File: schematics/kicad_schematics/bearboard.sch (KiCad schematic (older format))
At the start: 61 parts

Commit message: Added new joy stick to the misc library and schematic
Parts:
- removed P?: CONN_10X2, symbol CONN_10X2
- removed R? (x4): 0, symbol R
- added C? (x5): 100nF, symbol C
- added D? (x4): LED, symbol LED
- added JP? (x2): CONN_3, symbol CONN_3
- added P?: KOBICONN, symbol JACK-PMS
- added R? (x4): 690?, symbol R
- added R? (x5): 10K, symbol R
- added R? (x5): 0, symbol R
- added U?: TACT-SKQU, symbol TACT-SKQU
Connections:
- net labels added: JOY_CENTER, JOY_DOWN, JOY_LEFT, JOY_RIGHT, JOY_UP, LED0, LED1, LED2, LED3, WIZ_BRDY3
- net labels removed: +3.3V, TRACE_CK, TRACE_D0, TRACE_D1, TRACE_D2, TRACE_D3, WIZ_BRD3
- wire segments 498 -> 523
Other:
- note added: "GPIO LEDs"
- note added: "GPS CONNECTOR"
- note added: "JOYSTICK_BUTTONS"
- note added: "Optional UART2 Connector"
- note added: "POWER SUPPLY"
- note removed: "CN10 will suppot both legacy JTAG and\nfuture JTAG by 0 ohm resistors."
- note removed: "TRACE CONNECTOR"
- moved on the sheet: D?, P?, R?, U?

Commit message: Cleaned up Schematic File and modified SD card module, bearboard schematic
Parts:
- removed SW? (x2): SWITCH_INV, symbol SWITCH_INV
- removed U?: SD_CARD, symbol SD_CARD
- added JP?: CONN_3, symbol CONN_3
- added SW5, SW6: SWITCH, symbol SWITCH
- added U14: SD_CARD, symbol SD_CARD
- gave numbers to parts that had none: 80
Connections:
- net labels added: ARD_SH_AREF, ARD_SH_GP_4, ARD_SH_GP_5, ARD_SH_GP_6, ARD_SH_GP_7, ARD_SH_GP_8, ARD_SH_GP_9, BOOT0, BOOT1, USB5V, USBFTDI5V, VREF+, VREF-
- net labels removed: A, USBFTDI, USBPWR
- wire segments 523 -> 536
- no-connect marks 5 -> 6
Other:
- note added: "ANALOG POWER SUPPLY"
- note added: "ARM ST103F MICROCONTROLLER"
- note added: "BATTERY CONNECTOR"
- note added: "BOOT SWITCHES"
- note added: "FTDI PROGRAM INTERFACE"
- note added: "MAIN CRYSTAL"
- note added: "PORT GPIO"
- note added: "REAL-TIME CLOCK"
- note added: "RESET SWITCH"
- note added: "USB SLAVE INTERFACE"
- note added: "WIZNET NETWORK INTERFACE"
- moved on the sheet: C1, C10, C11, C12, C13, C2, C3, C4, C5, C6, C7, C8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

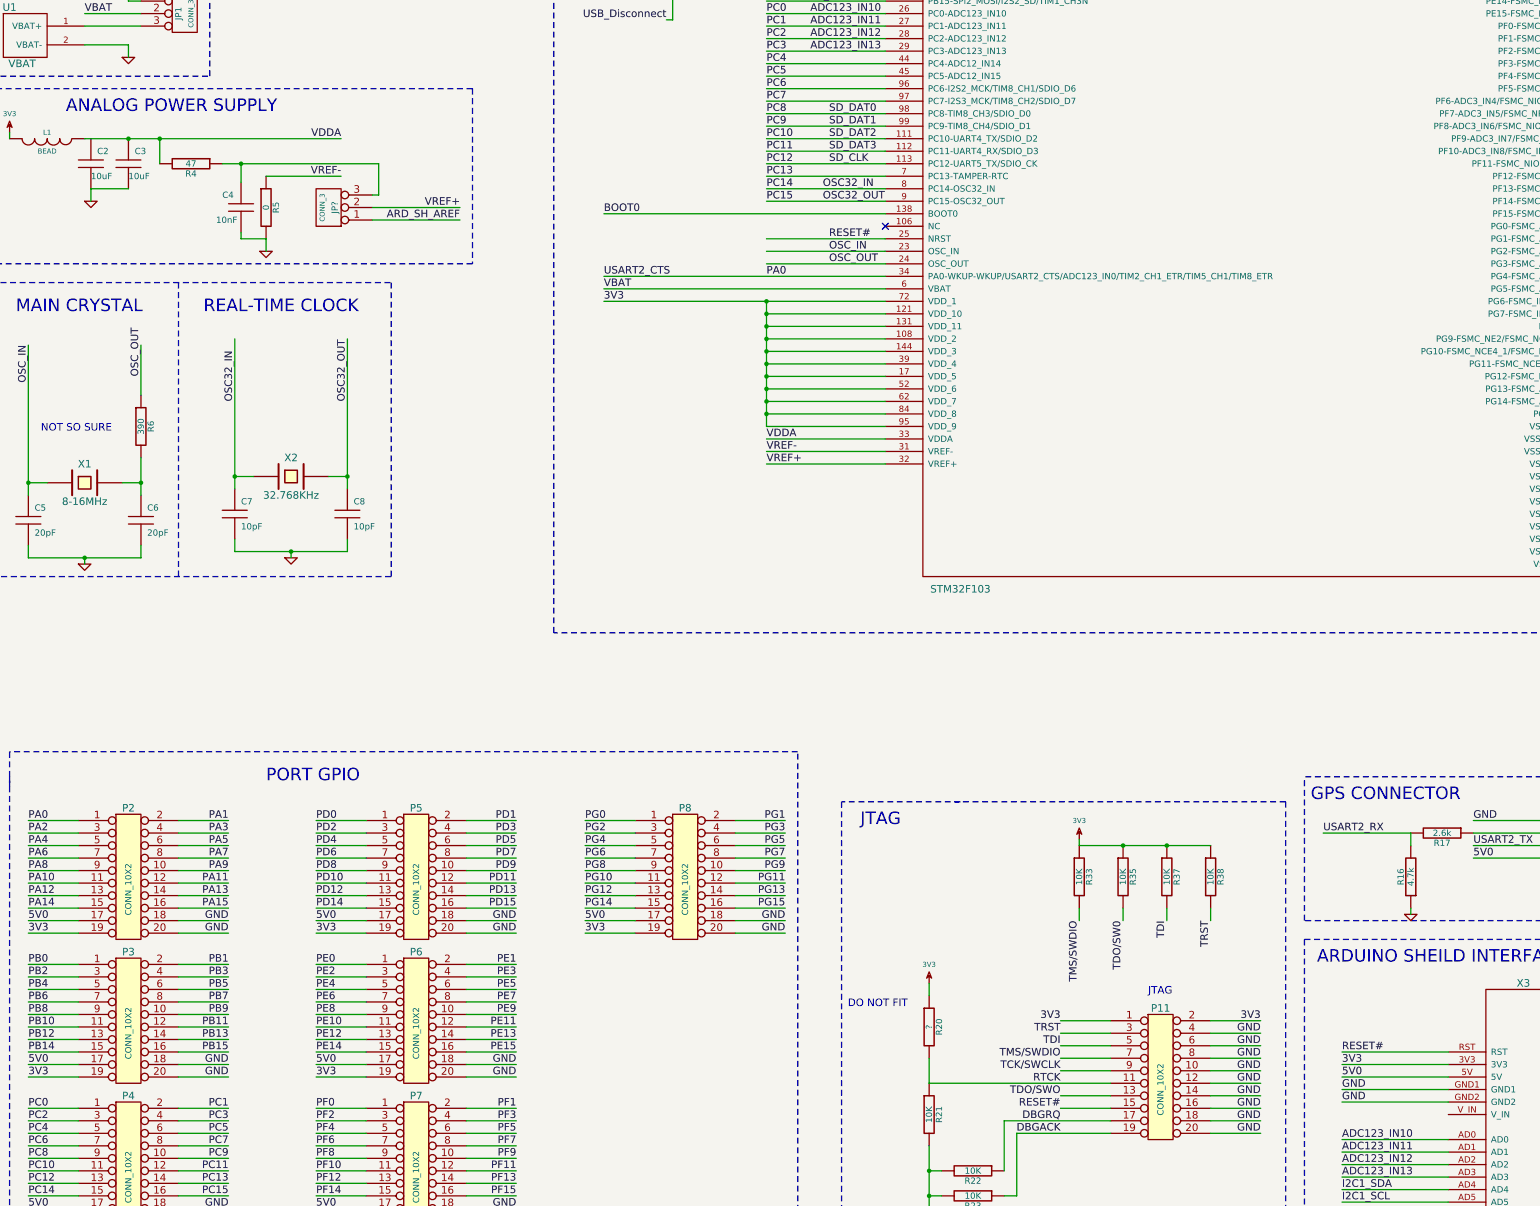
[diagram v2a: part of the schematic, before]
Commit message: Updated USB connector to change the sheild pin to power input Updated the schematic to fix some schematic electrical issues
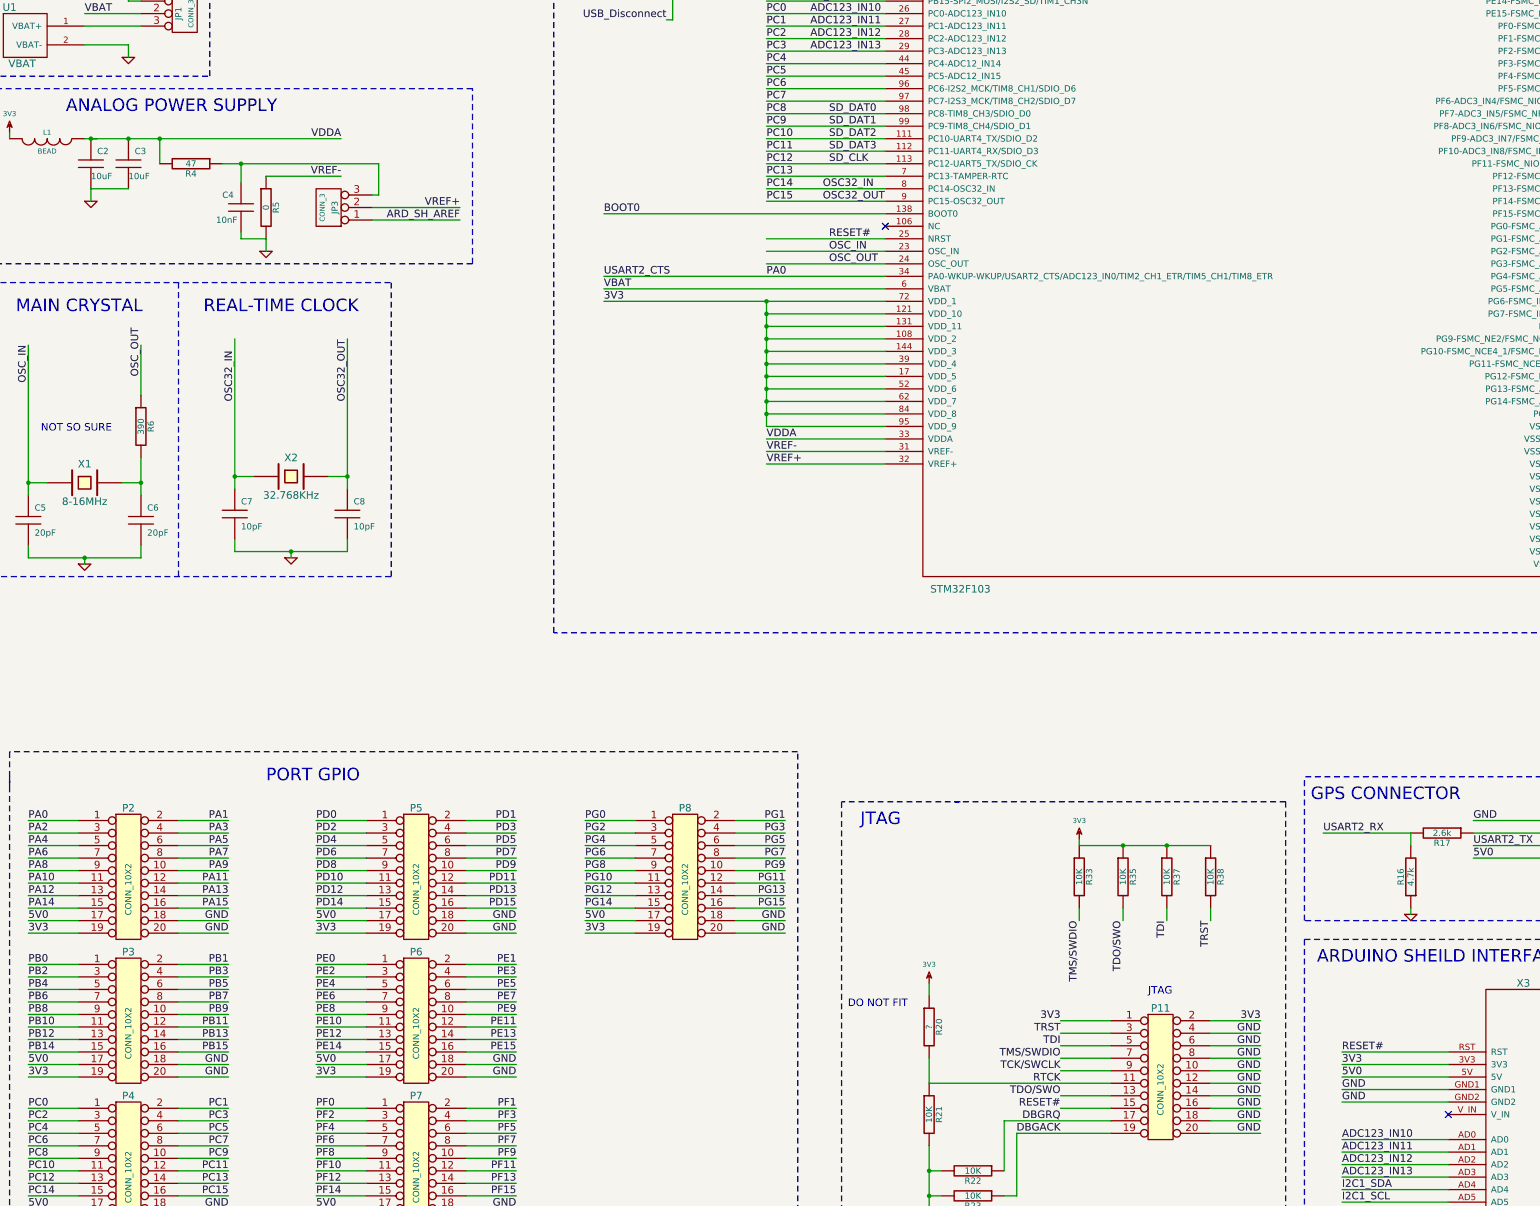
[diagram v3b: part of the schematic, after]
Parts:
- gave numbers to parts that had none: 1
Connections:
- net TDO/SW0 is gone; now on net PB3: R35.2
- net VDDA: now also C2.1
- no-connect marks 6 -> 7
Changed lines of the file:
@@
-EESchema Schematic File Version 2  date Wed 10 Mar 2010 05:32:05 PM EST
+EESchema Schematic File Version 2  date Wed 10 Mar 2010 08:20:30 PM EST
 LIBS:power
 LIBS:device
@@
 Sheet 1 5
 Title "BearBoard STM32F103"
-Date "10 mar 2010"
+Date "11 mar 2010"
 Rev "0"
 Comp "University of Maine"
@@
 Comment4 ""
 $EndDescr
+Text Label 9650 13600 3    60   ~ 0
+TDO/SWO
+Wire Wire Line
+	9650 13500 9650 13600
 Wire Notes Line
 	4450 8350 600  8350
 Wire Notes Line
-	4450 6950 4450 8350
+	4450 8350 4450 6950
 Wire Notes Line
 	4450 6950 600  6950
@@
 	10350 13600 10350 13500
 Wire Wire Line
-	9650 13600 9650 13500
-Wire Wire Line
 	9300 13600 9300 13500
 Connection ~ 10000 13000
@@
 Wire Wire Line
 	3650 8000 4350 8000
+Wire Wire Line
+	1400 7350 1450 7350
+Connection ~ 1400 7350
+NoConn ~ 12250 15150
 Text Label 4350 8000 2    60   ~ 0
 ARD_SH_AREF
 $Comp
-L CONN_3 JP?
+L CONN_3 JP3
 U 1 1 4B981D76
 P 3300 7900
-F 0 "JP?" V 3250 7900 50  0000 C CNN
+F 0 "JP3" V 3250 7900 50  0000 C CNN
 F 1 "CONN_3" V 3350 7900 40  0000 C CNN
 	1    3300 7900
@@
 Text Label 10350 13600 3    60   ~ 0
 TRST
-Text Label 9650 13600 3    60   ~ 0
-TDO/SW0
 Text Label 9300 13600 3    60   ~ 0
 TMS/SWDIO

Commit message: back annotated footprints into eeschem schematic
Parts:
- C1, C10, C11, C12, C13, C2, C3, C4, C5, C6, C7, C8, C9, R1, R10, R11, R12, R13, R14, R15, R16, R17, R18, R19, R2, R20, R21, R22, R23, R24, R25, R26, R27, R28, R29, R3, R30, R31, R32, R33, R34, R35, R36, R37, R38, R4, R5, R6, R7, R8, R9: footprint (none) -> SM0805
- D4, D5, D6, D7: footprint (none) -> LED-0805
- JP1, JP2, JP3: footprint (none) -> PIN_ARRAY_3X1
- P10: footprint (none) -> PIN_ARRAY_4x1
- P11, P2, P3, P4, P5, P6, P7, P8: footprint (none) -> PIN_ARRAY_10X2
- P9: footprint (none) -> PIN_ARRAY_7X1
- U2: footprint (none) -> LQFP144
- U3: footprint (none) -> alps_tact_button
- U4: footprint (none) -> EM406

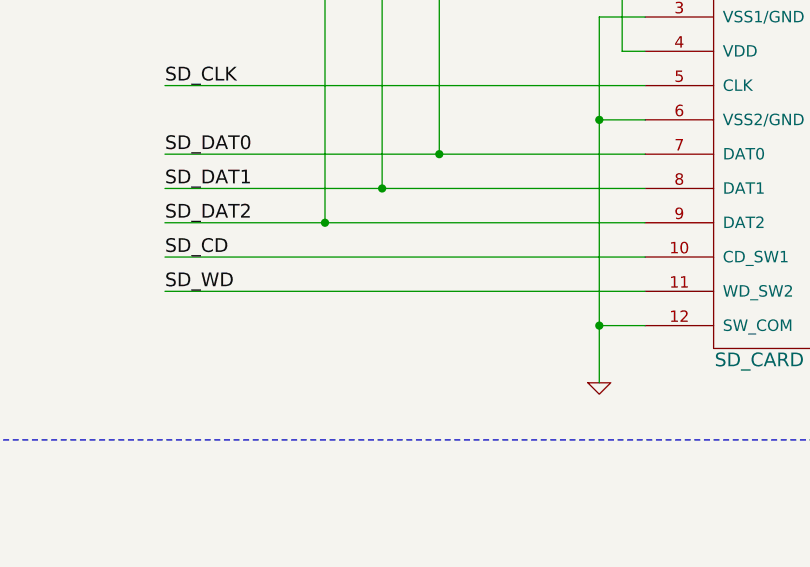
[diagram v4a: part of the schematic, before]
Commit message: added datasheets for cyrstals and aurdino sheild stuff
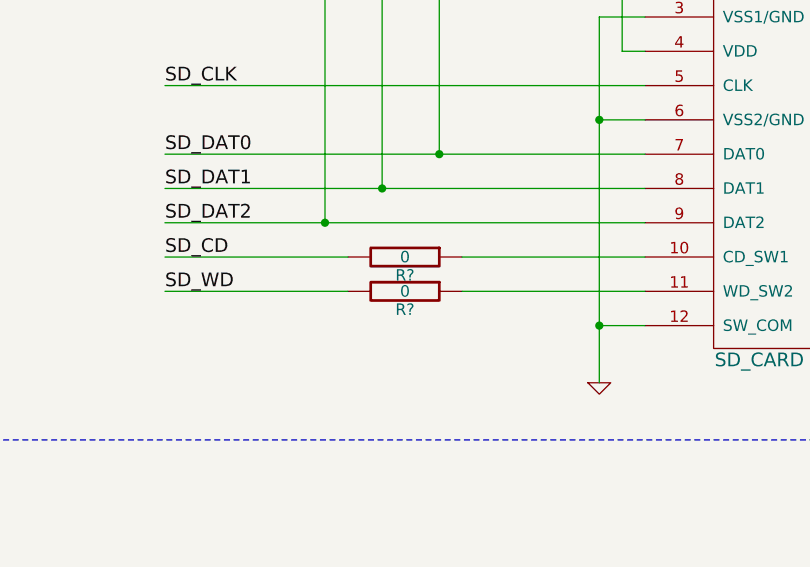
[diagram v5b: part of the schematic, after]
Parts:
- added R? (x2): 0, SM0805, symbol R
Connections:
- net PD13: now also R?.2; no longer U14.11 (WD_SW2)
- net PD3: now also R?.2; no longer U14.10 (CD_SW1)
- new net: R?.1, U14.10 (CD_SW1)
- new net: R?.1, U14.11 (WD_SW2)
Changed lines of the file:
@@
-EESchema Schematic File Version 2  date Fri 12 Mar 2010 11:31:07 AM EST
+EESchema Schematic File Version 2  date Sat 13 Mar 2010 12:50:25 PM EST
 LIBS:power
 LIBS:device
@@
 Sheet 1 5
 Title "BearBoard STM32F103"
-Date "11 mar 2010"
+Date "13 mar 2010"
 Rev "0"
 Comp "University of Maine"
@@
 Comment4 ""
 $EndDescr
-Text Label 9650 13600 3    60   ~ 0
-TDO/SWO
+Wire Wire Line
+	18600 11200 17800 11200
+Wire Wire Line
+	19100 11200 19900 11200
 Wire Wire Line
 	9650 13500 9650 13600
@@
 	7750 7450 6800 7450
 Wire Wire Line
-	17800 11200 19900 11200
-Wire Wire Line
 	17800 10900 19900 10900
 Wire Wire Line
@@
 	17800 10750 19900 10750
 Wire Wire Line
-	17800 11050 19900 11050
-Wire Wire Line
 	6800 7550 7750 7550
 Wire Wire Line
@@
 	1400 7350 1450 7350
 Connection ~ 1400 7350
+Wire Wire Line
+	19900 11050 19100 11050
+Wire Wire Line
+	18600 11050 17800 11050
+$Comp
+L R R?
+U 1 1 4B9BD03D
+P 18850 11200
+F 0 "R?" V 18930 11200 50  0000 C CNN
+F 1 "0" V 18850 11200 50  0000 C CNN
+F 2 "SM0805" H 18850 11200 60  0001 C CNN
+	1    18850 11200
+	0    1    1    0
+$EndComp
+$Comp
+L R R?
+U 1 1 4B9BD039
+P 18850 11050
+F 0 "R?" V 18930 11050 50  0000 C CNN
+F 1 "0" V 18850 11050 50  0000 C CNN
+F 2 "SM0805" H 18850 11050 60  0001 C CNN
+	1    18850 11050
+	0    1    1    0
+$EndComp
+Text Label 9650 13600 3    60   ~ 0
+TDO/SWO
 NoConn ~ 12250 15150
 Text Label 4350 8000 2    60   ~ 0
